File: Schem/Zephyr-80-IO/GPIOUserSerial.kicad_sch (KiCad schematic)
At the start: 7 parts, among them J4 Conn_02x10_Odd_Even, U8 MAX202IDR

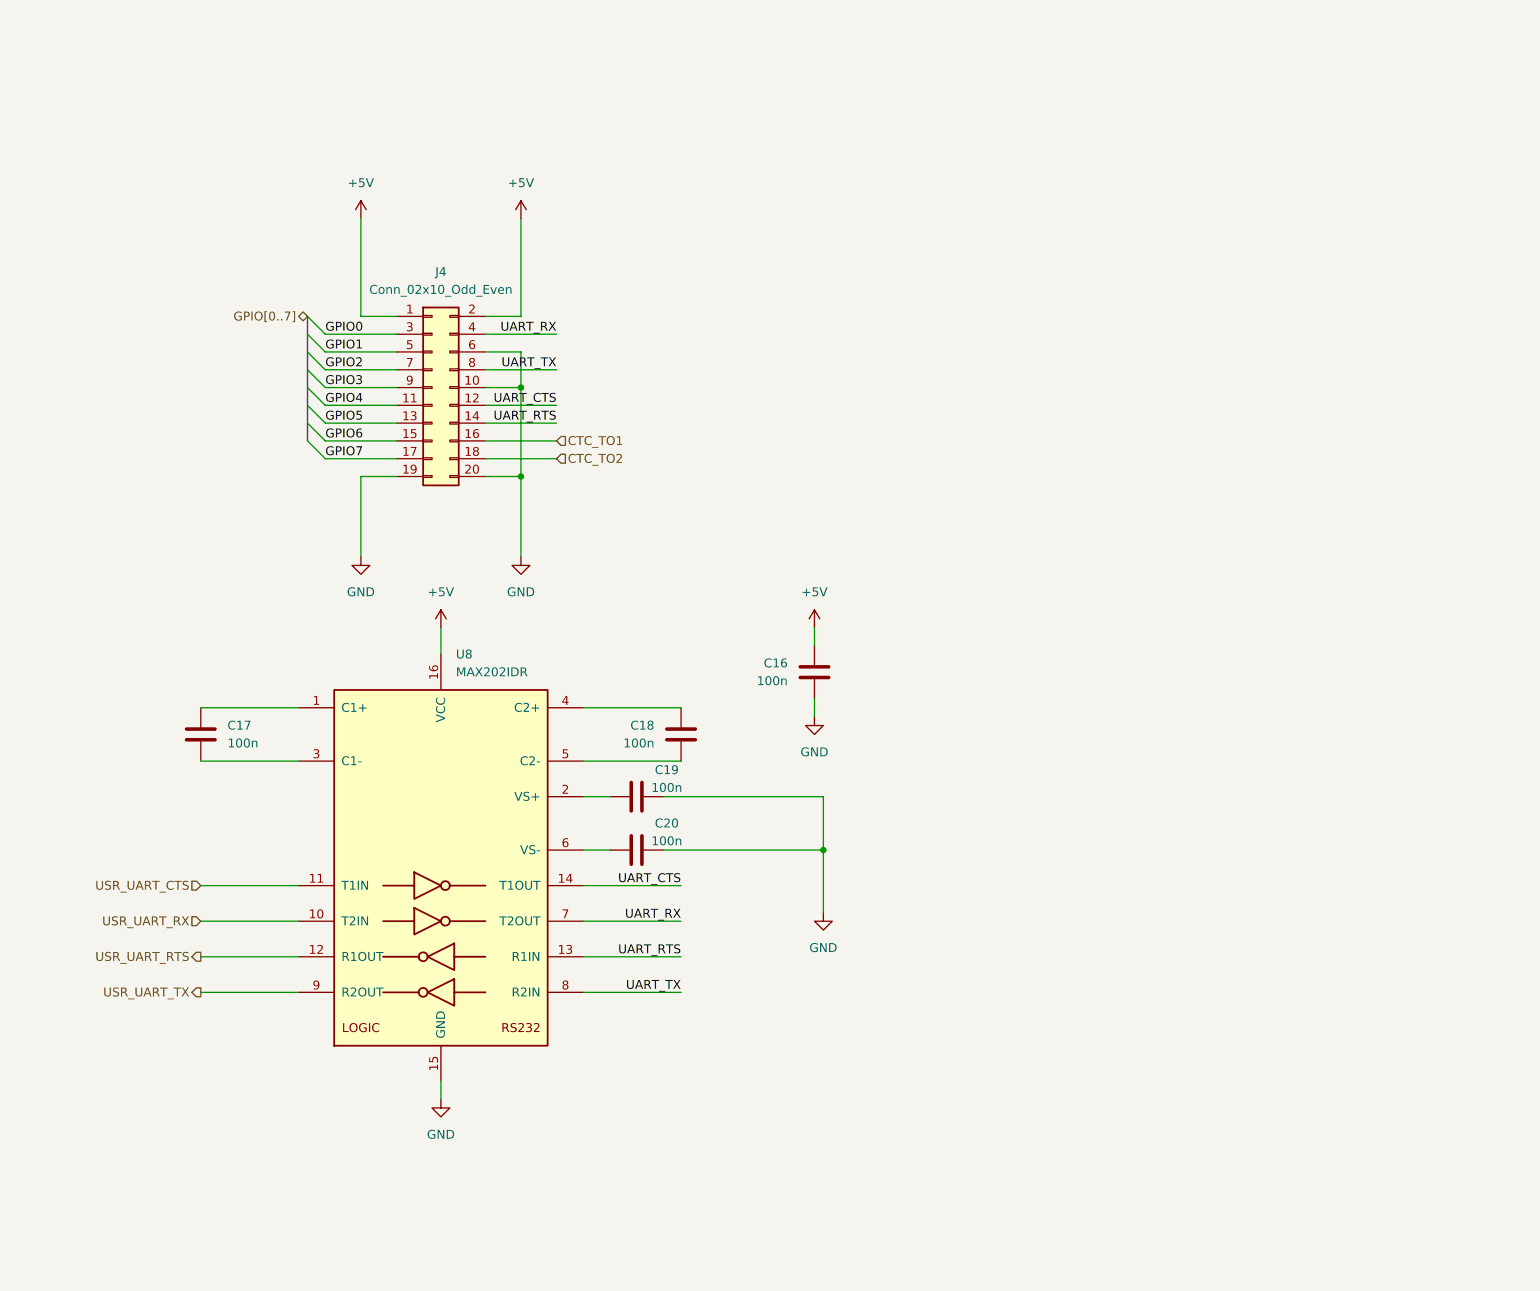
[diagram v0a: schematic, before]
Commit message: Completed the IO Controller schematic and PCB layout for the Zephyr-80 project. This includes the design of the Baud Clock, CPU Address Decoding, Console Port, Device Select Decode, GPIO User Serial, and the main IO Controller schematics. Additionally, the PCB layout for the Zephyr-80 IO board has been created, along with the necessary library files and documentation for the control signal mapping.
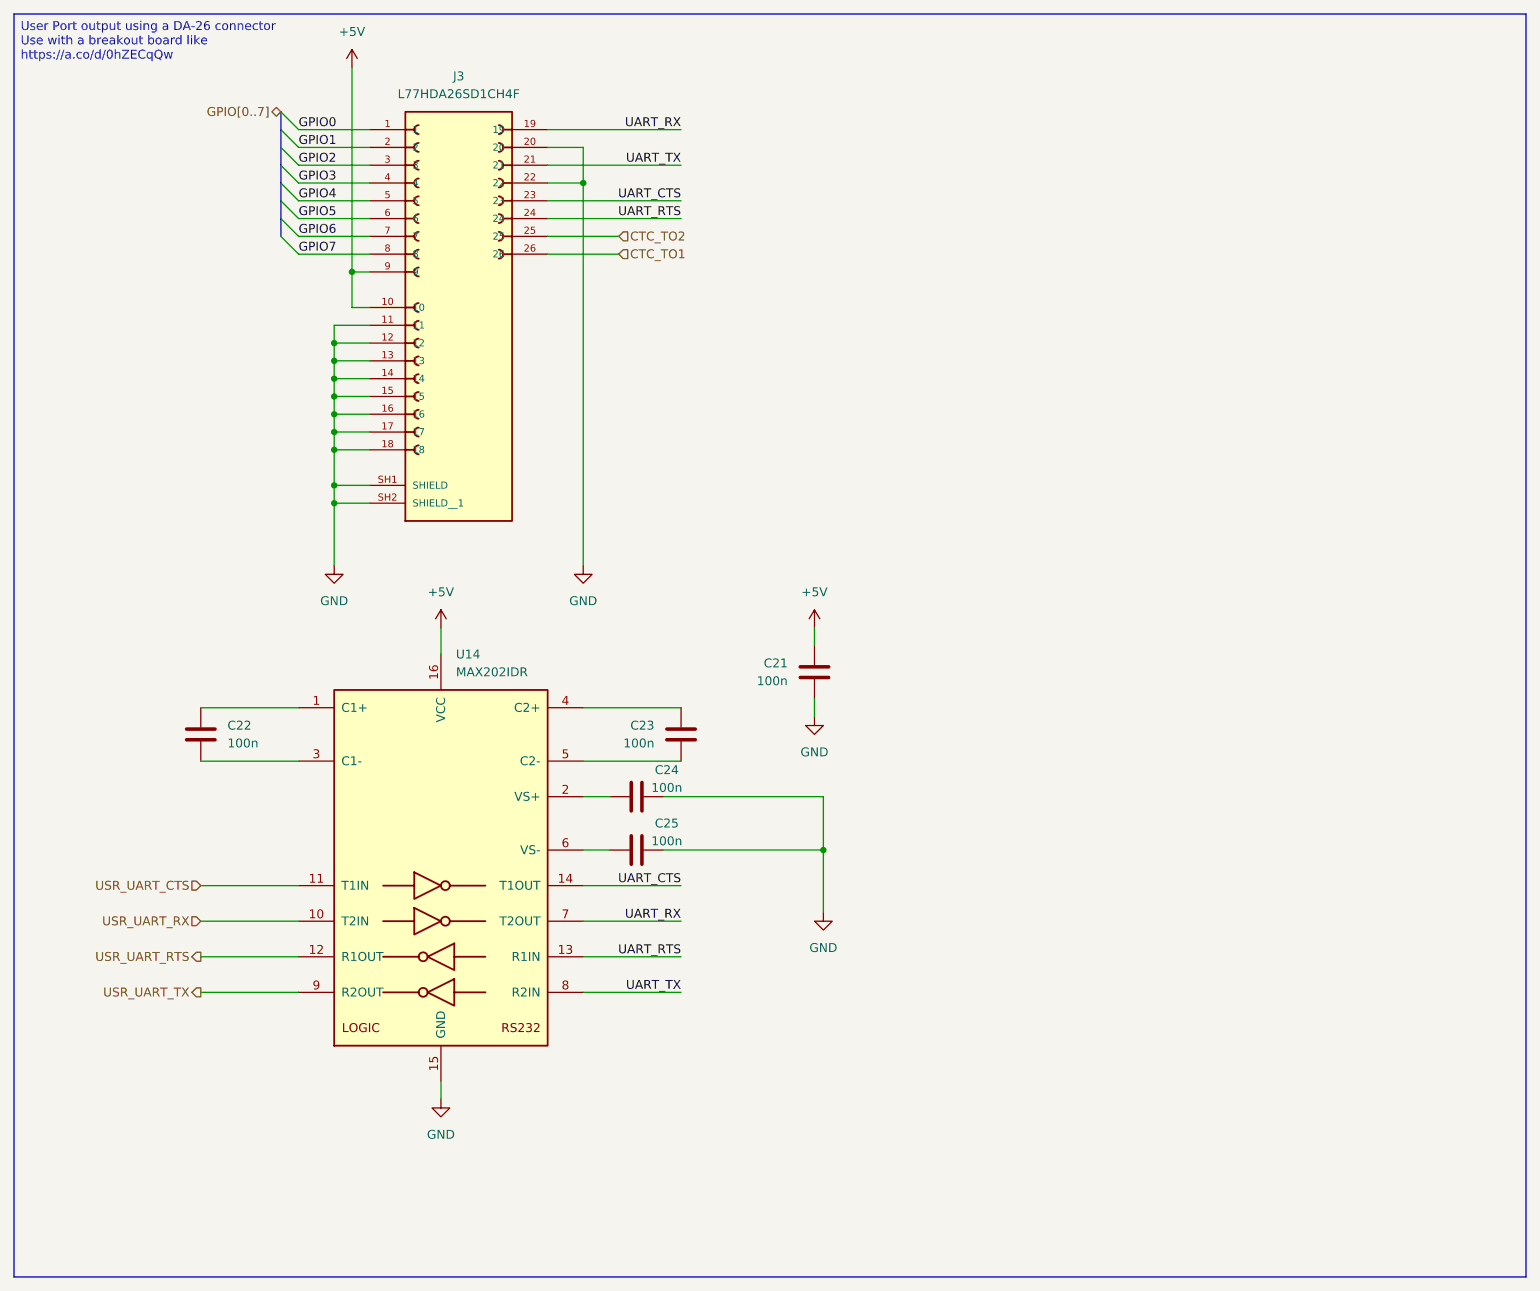
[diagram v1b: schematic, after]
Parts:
- removed J4: Conn_02x10_Odd_Even, Connector_IDC:IDC-Header_2x10_P2.54mm_Vertical, symbol Connector_Generic:Conn_02x10_Odd_Even
- added J3: L77HDA26SD1CH4F, Footprints:AMPHENOL_L77HDA26SD1CH4F, symbol L77HDA26SD1CH4F:L77HDA26SD1CH4F
- renumbered C16 to C21, C17 to C22, C18 to C23, C19 to C24, C20 to C25, U8 to U14
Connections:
- net +5V: now also J3.10, J3.9
- net CTC_TO1: now also J3.26
- net CTC_TO2: now also J3.25
- net GND: now also J3.11, J3.12, J3.13, J3.14, J3.15, J3.16, J3.17, J3.18, J3.20, J3.22, J3.SH1 (SHIELD), J3.SH2 (SHIELD__1)
- net GPIO0: now also J3.1
- net GPIO1: now also J3.2
- net GPIO2: now also J3.3
- net GPIO3: now also J3.4
- net GPIO4: now also J3.5
- net GPIO5: now also J3.6
- net GPIO6: now also J3.7
- net GPIO7: now also J3.8
- net UART_CTS: now also J3.23
- net UART_RTS: now also J3.24
- net UART_RX: now also J3.19
- net UART_TX: now also J3.21

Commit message: Added all the manufacturer part numbers to the KiCad schematics and PCB files. This will make it easier to order the parts for the project and ensure that the correct components are used. I also removed some of the old schematics that were no longer needed, such as the BaudClock, ConsolePort, DeviceSelectDecode, GPIOUserSerial, IO Controller, UserPorts, Video, and Z80HomeBrew schematics. These changes will help to streamline the design and make it easier to understand.
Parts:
- J3: MANUFACTURER_PART_NUMBER (none) -> L77HDA26SD1CH4F
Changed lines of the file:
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@@
+			)
+		)
+		(property "MANUFACTURER_PART_NUMBER" "L77HDA26SD1CH4F"
+			(at 78.74 57.15 0)
+			(effects
+				(font
+					(size 1.27 1.27)
+				)
+				(hide yes)
 			)
 		)
